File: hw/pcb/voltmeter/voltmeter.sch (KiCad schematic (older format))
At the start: 14 parts, among them J0 Screw_Terminal_01x02, K0 SPST Relay, K1 SPST Relay, K3 SPST Relay

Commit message: Updated circuit, added components, demo PCB layout. w/ Adam
Picked some parts and added them to the circuit. Implemented ADC circuit suggested by Nick.
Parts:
- removed D4: Red LED, symbol Device:LED
- removed K0, K1, K3: SPST Relay, symbol Relay:DIPxx-1Axx-11x
- removed R4: R, symbol Device:R
- removed U?: CA56-12EWA, Display_7Segment:CA56-12EWA, symbol Display_Character:CA56-12EWA
- added D3-x2, D3-x3: Green LED, symbol Device:LED
- added Q1, Q2: 2N7000, digikey-footprints:TO-92-3, symbol dk_Transistors-FETs-MOSFETs-Single:2N7000
- added R3-x2, R3-x3: R, symbol Device:R
- added U1: SN74HC595N, digikey-footprints:DIP-16_W7.62mm, symbol dk_Logic-Shift-Registers:SN74HC595N
- R1: value 20k -> 5k
- R2: value 49.9k -> 2k
- renumbered D3-x to D3-x1, R3-x to R3-x1
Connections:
- net labels added: 15vLeg, 30vLeg, 5vLeg, ADC
- wire segments 22 -> 31
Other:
- moved on the sheet: R3-x1

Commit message: Move to SMD parts; move to parts from Digikey library.
Move to SMD parts; move to parts from Digikey library. Schematic updates.
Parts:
- removed D0: 5.1V Zener, symbol Device:D_Zener
- removed D3-x1, D3-x2, D3-x3: Green LED, symbol Device:LED
- removed J0: Screw_Terminal_01x02, symbol Connector:Screw_Terminal_01x02
- removed Q1, Q2: 2N7000, digikey-footprints:TO-92-3, symbol dk_Transistors-FETs-MOSFETs-Single:2N7000
- removed U1: SN74HC595N, digikey-footprints:DIP-16_W7.62mm, symbol dk_Logic-Shift-Registers:SN74HC595N
- added D3-1, D3-2, D3-3: LTST-C150TBKT, digikey-footprints:1206, symbol dk_LED-Indication-Discrete:LTST-C150TBKT
- added J0: 1935161, digikey-footprints:Terminal_Block_D1.3mm_P5mm, symbol dk_Terminal-Blocks-Wire-to-Board:1935161
- added Q1, Q2: 2N7002, digikey-footprints:SOT-23-3, symbol dk_Transistors-FETs-MOSFETs-Single:2N7002
- R0, R1, R2: footprint (none) -> Resistor_SMD:R_0805_2012Metric_Pad1.15x1.40mm_HandSolder
- R3-1: renamed from R3-x1; value R -> 86.6; footprint (none) -> Resistor_SMD:R_0805_2012Metric_Pad1.15x1.40mm_HandSolder
- R3-2: renamed from R3-x2; value R -> 86.6; footprint (none) -> Resistor_SMD:R_0805_2012Metric_Pad1.15x1.40mm_HandSolder
- R3-3: renamed from R3-x3; value R -> 86.6; footprint (none) -> Resistor_SMD:R_0805_2012Metric_Pad1.15x1.40mm_HandSolder
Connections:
- net labels added: VoltageDivider

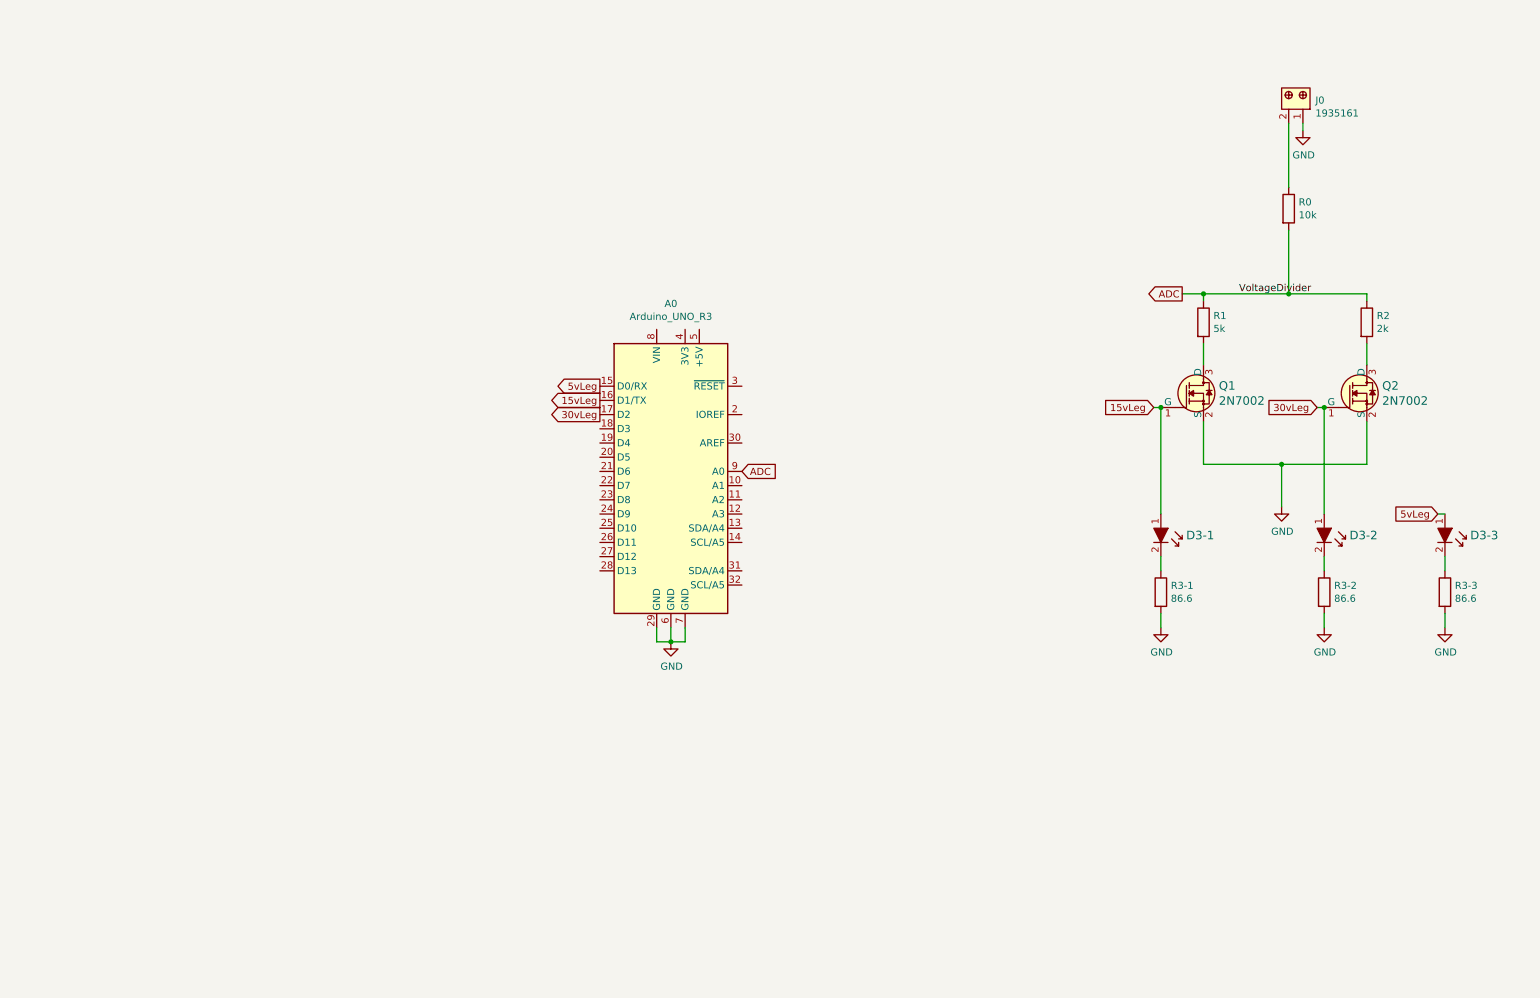
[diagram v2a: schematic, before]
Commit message: Changed to 4 voltage scales.
Changed design from 3-scale to 4-scale. Selected a few more parts and added them to the schematic.
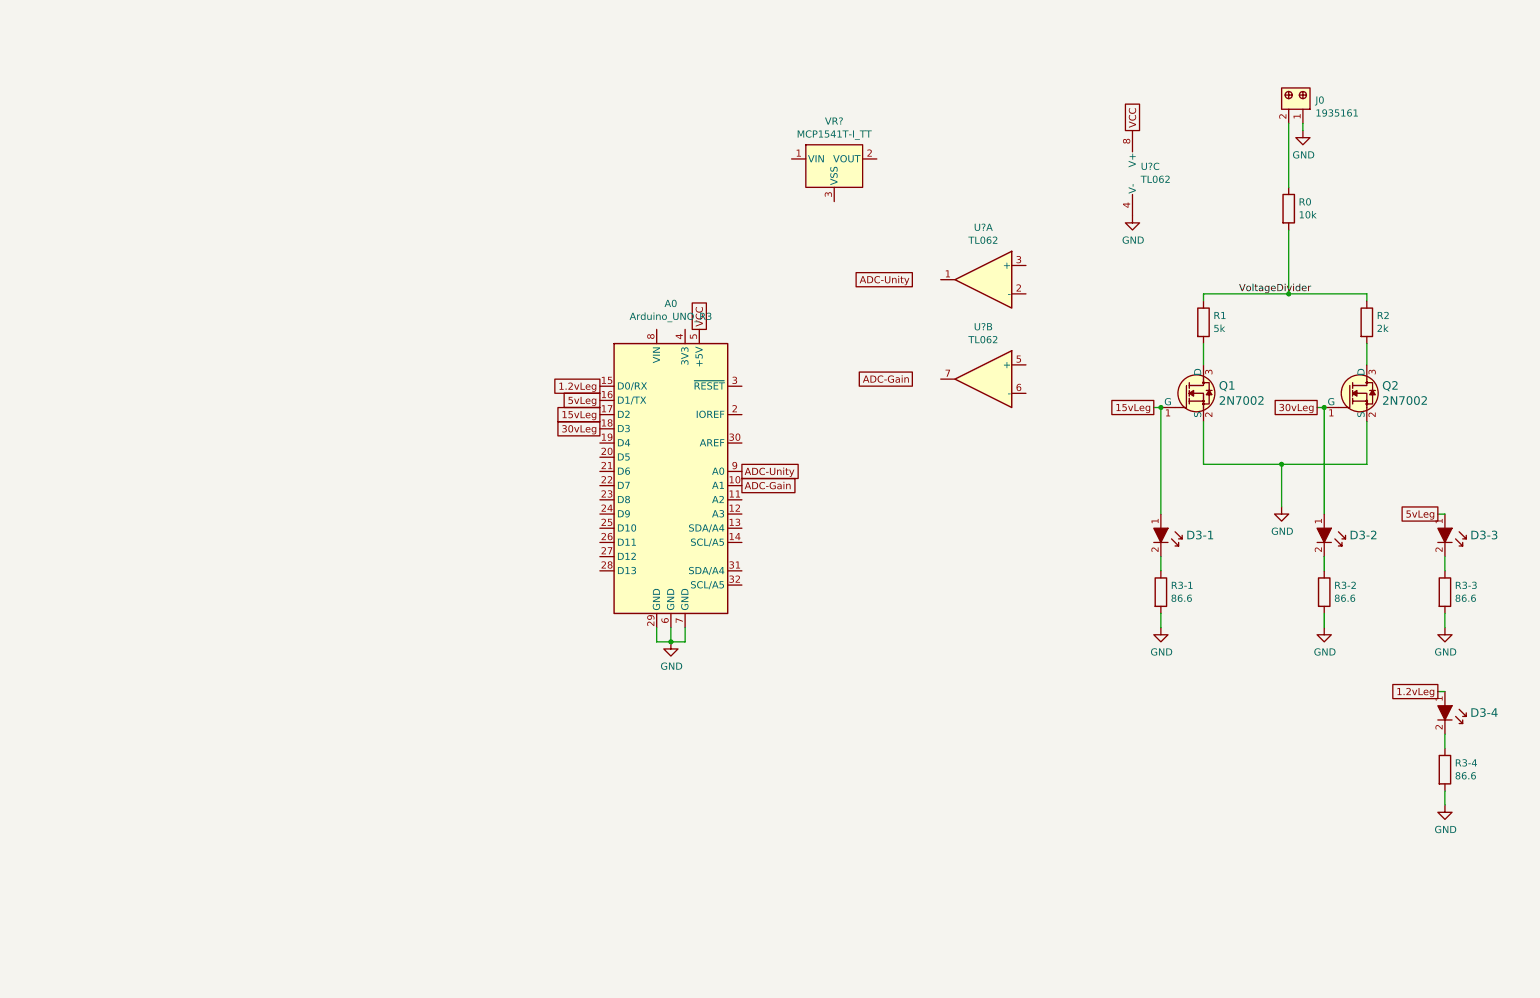
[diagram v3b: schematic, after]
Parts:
- added D3-4: LTST-C150TBKT, digikey-footprints:1206, symbol dk_LED-Indication-Discrete:LTST-C150TBKT
- added R3-4: 86.6, Resistor_SMD:R_0805_2012Metric_Pad1.15x1.40mm_HandSolder, symbol Device:R
- added U? (x3): TL062, footprints:TL062CDR, symbol Amplifier_Operational:TL062
- added VR?: MCP1541T-I_TT, digikey-footprints:SOT-23-3, symbol dk_PMIC-Voltage-Reference:MCP1541T-I_TT
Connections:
- net 15vLeg: now also A0.17 (D2); no longer A0.16 (D1/TX)
- net 30vLeg: now also A0.18 (D3); no longer A0.17 (D2)
- net 5vLeg: now also A0.16 (D1/TX); no longer A0.15 (D0/RX)
- net GND: now also R3-4.2, U?.4 (V-)
- net ADC-Gain: now reaches A0.10 (A1)
- net VCC: now reaches A0.5 (+5V)
- net VCC: now also U?.8 (V+)
- net ADC renamed VoltageDivider
- net VoltageDivider: no longer A0.9 (A0)
- new net: D3-4.2, R3-4.1
- new net 1.2vLeg: A0.15 (D0/RX), D3-4.1
- new net ADC-Unity: A0.9 (A0)
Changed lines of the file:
@@
 Wire Wire Line
 	8650 2850 8650 3600
-Text GLabel 8600 2850 0    50   Input ~ 0
+Text GLabel 8600 2850 0    50   UnSpc ~ 0
 15vLeg
-Text GLabel 9750 2850 0    50   Input ~ 0
+Text GLabel 9750 2850 0    50   UnSpc ~ 0
 30vLeg
-Text GLabel 4700 2800 0    50   Output ~ 0
+Text GLabel 4700 2900 0    50   UnSpc ~ 0
 15vLeg
-Text GLabel 4700 2900 0    50   Output ~ 0
+Text GLabel 4700 3000 0    50   UnSpc ~ 0
 30vLeg
 $Comp
@@
 Wire Wire Line
 	10650 3900 10650 4000
-Text GLabel 10600 3600 0    50   Input ~ 0
+Text GLabel 10600 3600 0    50   UnSpc ~ 0
 5vLeg
-Text GLabel 4700 2700 0    50   Output ~ 0
+Text GLabel 4700 2800 0    50   UnSpc ~ 0
 5vLeg
 Wire Wire Line
 	9550 1300 9550 850
-Text GLabel 8800 2050 0    50   Output ~ 0
-ADC
-Text GLabel 5700 3300 2    50   Input ~ 0
-ADC
-Wire Wire Line
-	8800 2050 8950 2050
-Connection ~ 8950 2050
+Text GLabel 6900 1950 0    50   UnSpc ~ 0
+ADC-Unity
+Text GLabel 5700 3300 2    50   UnSpc ~ 0
+ADC-Unity
 Wire Wire Line
 	8600 2850 8650 2850
@@
 Text Label 9200 2050 0    50   ~ 0
 VoltageDivider
+$Comp
+L dk_PMIC-Voltage-Reference:MCP1541T-I_TT VR?
+U 1 1 5F4868C2
+P 6350 1100
+F 0 "VR?" H 6350 1365 50  0000 C CNN
+F 1 "MCP1541T-I_TT" H 6350 1274 50  0000 C CNN
+F 2 "digikey-footprints:SOT-23-3" H 6550 1300 60  0001 L CNN
+F 3 "http://www.microchip.com/mymicrochip/filehandler.aspx?ddocname=en011331" H 6550 1400 60  0001 L CNN
+F 4 "MCP1541T-I/TTCT-ND" H 6550 1500 60  0001 L CNN "Digi-Key_PN"
+F 5 "MCP1541T-I/TT" H 6550 1600 60  0001 L CNN "MPN"
+F 6 "Integrated Circuits (ICs)" H 6550 1700 60  0001 L CNN "Category"
+F 7 "PMIC - Voltage Reference" H 6550 1800 60  0001 L CNN "Family"
+F 8 "http://www.microchip.com/mymicrochip/filehandler.aspx?ddocname=en011331" H 6550 1900 60  0001 L CNN "DK_Datasheet_Link"
+F 9 "/product-detail/en/microchip-technology/MCP1541T-I-TT/MCP1541T-I-TTCT-ND/1979818" H 6550 2000 60  0001 L CNN "DK_Detail_Page"
+F 10 "IC VREF SERIES 4.096V SOT23-3" H 6550 2100 60  0001 L CNN "Description"
+F 11 "Microchip Technology" H 6550 2200 60  0001 L CNN "Manufacturer"
+F 12 "Active" H 6550 2300 60  0001 L CNN "Status"
+	1    6350 1100
+	1    0    0    -1
+$EndComp
+$Comp
+L power:GND #PWR0107
+U 1 1 5F4BD11F
+P 8450 1500
+F 0 "#PWR0107" H 8450 1250 50  0001 C CNN
+F 1 "GND" H 8455 1327 50  0000 C CNN
+F 2 "" H 8450 1500 50  0001 C CNN
+F 3 "" H 8450 1500 50  0001 C CNN
+	1    8450 1500
+	1    0    0    -1
+$EndComp
+Text GLabel 5400 2300 1    50   UnSpc ~ 0
+VCC
+Text GLabel 8450 900  1    50   UnSpc ~ 0
+VCC
+$Comp
+L Device:R R3-4
+U 1 1 5F4CB52D
+P 10650 5400
+F 0 "R3-4" H 10720 5446 50  0000 L CNN
+F 1 "86.6" H 10720 5355 50  0000 L CNN
+F 2 "Resistor_SMD:R_0805_2012Metric_Pad1.15x1.40mm_HandSolder" V 10580 5400 50  0001 C CNN
+F 3 "~" H 10650 5400 50  0001 C CNN
+	1    10650 5400
+	1    0    0    -1
+$EndComp
+$Comp
+L power:GND #PWR0108
+U 1 1 5F4CB533
+P 10650 5650
+F 0 "#PWR0108" H 10650 5400 50  0001 C CNN
+F 1 "GND" H 10655 5477 50  0000 C CNN
+F 2 "" H 10650 5650 50  0001 C CNN
+F 3 "" H 10650 5650 50  0001 C CNN
+	1    10650 5650
+	1    0    0    -1
+$EndComp
+Wire Wire Line
+	10650 5550 10650 5650
+Wire Wire Line
+	10650 5150 10650 5250
+Text GLabel 10600 4850 0    50   UnSpc ~ 0
+1.2vLeg
+Wire Wire Line
+	10600 4850 10650 4850
+$Comp
+L dk_LED-Indication-Discrete:LTST-C150TBKT D3-4
+U 1 1 5F4CB546
+P 10650 5050
+F 0 "D3-4" V 10600 5228 60  0000 L CNN
+F 1 "LTST-C150TBKT" V 10653 5228 60  0001 L CNN
+F 2 "digikey-footprints:1206" H 10850 5250 60  0001 L CNN
+F 3 "http://optoelectronics.liteon.com/upload/download/DS22-2000-026/LTST-C150TBKT(0630).pdf" H 10850 5350 60  0001 L CNN
+F 4 "160-1643-1-ND" H 10850 5450 60  0001 L CNN "Digi-Key_PN"
+F 5 "LTST-C150TBKT" H 10850 5550 60  0001 L CNN "MPN"
+F 6 "Optoelectronics" H 10850 5650 60  0001 L CNN "Category"
+F 7 "LED Indication - Discrete" H 10850 5750 60  0001 L CNN "Family"
+F 8 "http://optoelectronics.liteon.com/upload/download/DS22-2000-026/LTST-C150TBKT(0630).pdf" H 10850 5850 60  0001 L CNN "DK_Datasheet_Link"
+F 9 "/product-detail/en/lite-on-inc/LTST-C150TBKT/160-1643-1-ND/573584" H 10850 5950 60  0001 L CNN "DK_Detail_Page"
+F 10 "LED BLUE CLEAR 1206 SMD" H 10850 6050 60  0001 L CNN "Description"
+F 11 "Lite-On Inc." H 10850 6150 60  0001 L CNN "Manufacturer"
+F 12 "Active" H 10850 6250 60  0001 L CNN "Status"
+	1    10650 5050
+	0    1    1    0
+$EndComp
+Text GLabel 4700 2700 0    50   UnSpc ~ 0
+1.2vLeg
+Text GLabel 5700 3400 2    50   UnSpc ~ 0
+ADC-Gain
+Text GLabel 6900 2650 0    50   UnSpc ~ 0
+ADC-Gain
+$Comp
+L Amplifier_Operational:TL062 U?
+U 1 1 5F4CF15C
+P 7400 1950
+F 0 "U?" H 7400 2317 50  0000 C CNN
+F 1 "TL062" H 7400 2226 50  0000 C CNN
+F 2 "footprints:TL062CDR" H 7400 1950 50  0001 C CNN
+F 3 "http://www.ti.com/lit/ds/symlink/tl061.pdf" H 7400 1950 50  0001 C CNN
+	1    7400 1950
+	-1   0    0    -1
+$EndComp
+$Comp
+L Amplifier_Operational:TL062 U?
+U 2 1 5F4D172B
+P 7400 2650
+F 0 "U?" H 7400 3017 50  0000 C CNN
+F 1 "TL062" H 7400 2926 50  0000 C CNN
+F 2 "footprints:TL062CDR" H 7400 2650 50  0001 C CNN
+F 3 "http://www.ti.com/lit/ds/symlink/tl061.pdf" H 7400 2650 50  0001 C CNN
+	2    7400 2650
+	-1   0    0    -1
+$EndComp
+$Comp
+L Amplifier_Operational:TL062 U?
+U 3 1 5F4D3B6F
+P 8550 1200
+F 0 "U?" H 8508 1246 50  0000 L CNN
+F 1 "TL062" H 8508 1155 50  0000 L CNN
+F 2 "footprints:TL062CDR" H 8550 1200 50  0001 C CNN
+F 3 "http://www.ti.com/lit/ds/symlink/tl061.pdf" H 8550 1200 50  0001 C CNN
+	3    8550 1200
+	1    0    0    -1
+$EndComp
 $EndSCHEMATC

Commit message: Finished the schematic!
Added 7-segment display, op-amps, and completed resistors and capacitors for ICs. First pass at the schematic is complete!
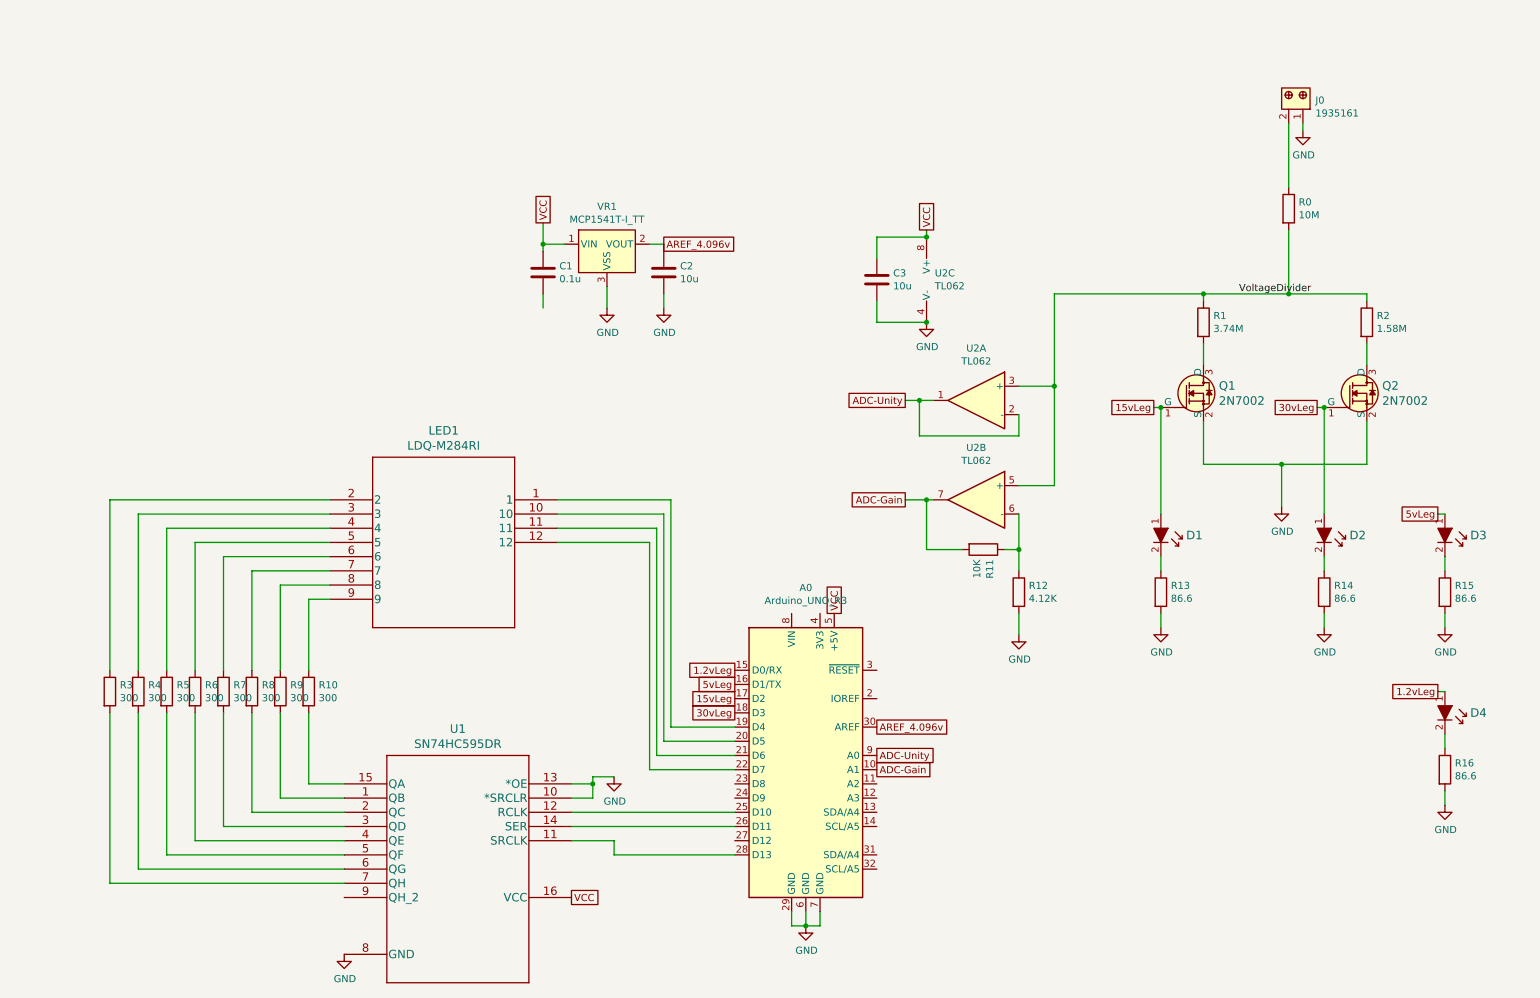
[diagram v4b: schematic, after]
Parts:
- added C1: 0.1u, Capacitor_SMD:C_0805_2012Metric_Pad1.15x1.40mm_HandSolder, symbol Device:C
- added C2, C3: 10u, Capacitor_SMD:C_0805_2012Metric_Pad1.15x1.40mm_HandSolder, symbol Device:C
- added LED1: LDQ-M284RI, footprints3:LDQ-M284RI, symbol 2020-08-31_02-39-33:LDQ-M284RI
- added R10, R3, R4, R5, R6, R7, R8, R9: 300, Resistor_SMD:R_0805_2012Metric_Pad1.15x1.40mm_HandSolder, symbol Device:R
- added R11: 10K, Resistor_SMD:R_0805_2012Metric_Pad1.15x1.40mm_HandSolder, symbol Device:R
- added R12: 4.12K, Resistor_SMD:R_0805_2012Metric_Pad1.15x1.40mm_HandSolder, symbol Device:R
- added U1: SN74HC595DR, footprints2:SN74HC595DR, symbol 2020-08-31_02-24-53:SN74HC595DR
- R0: value 10k -> 10M
- R1: value 5k -> 3.74M
- R2: value 2k -> 1.58M
- gave numbers to parts that had none: 2
- renumbered D3-1 to D1, D3-2 to D2, D3-3 to D3, D3-4 to D4, R3-1 to R13, R3-2 to R14, R3-3 to R15, R3-4 to R16
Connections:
- net ADC-Gain: now also U2.7, R11.2
- net ADC-Unity: now also U2.1, U2.2 (-)
- net GND: now also VR1.3 (VSS), C2.2, C3.2, R12.2, U1.10 (*SRCLR), U1.13 (*OE), U1.8 (GND)
- net VCC: now also VR1.1 (VIN), C1.1, C3.1, U1.16 (VCC)
- net VoltageDivider: now also U2.3 (+), U2.5 (+)
- net at A0.19 (D4): now also LED1.1
- net at A0.20 (D5): now also LED1.10
- net at A0.21 (D6): now also LED1.11
- net at A0.22 (D7): now also LED1.12
- net at A0.25 (D10): now also U1.12 (RCLK)
- net at A0.26 (D11): now also U1.14 (SER)
- net at A0.28 (D13): now also U1.11 (SRCLK)
- net AREF_4.096v: now reaches A0.30 (AREF)
- net AREF_4.096v: now also VR1.2 (VOUT), C2.1
- net at U2.6 (-): now also R11.1, R12.1
- new net: R9.2, U1.1 (QB)
- new net: R10.2, U1.15 (QA)
- new net: R8.2, U1.2 (QC)
- new net: R7.2, U1.3 (QD)
- new net: R6.2, U1.4 (QE)
- new net: R5.2, U1.5 (QF)
- new net: R4.2, U1.6 (QG)
- new net: R3.2, U1.7 (QH)
- new net: LED1.2, R3.1
- new net: LED1.3, R4.1
- new net: LED1.4, R5.1
- new net: LED1.5, R6.1
- new net: LED1.6, R7.1
- new net: LED1.7, R8.1
- new net: LED1.8, R9.1
- new net: LED1.9, R10.1
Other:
- moved on the sheet: A0, U2A, U2B, U2C, VR1

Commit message: Fix as many DRC errors as possible.
Fixed DRC errors by marking unused pins and editing pin directionality on some schematic symbols.
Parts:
- removed A0: Arduino_UNO_R3, Module:Arduino_UNO_R3, symbol MCU_Module:Arduino_UNO_R3
- added A0: Arduino_UNO_R3_SHIELD, Module:Arduino_UNO_R3, symbol marks_library:Arduino_UNO_R3_SHIELD
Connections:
- net 1.2vLeg: now also A0.15 (D0/RX)
- net 15vLeg: now also A0.17 (D2)
- net 30vLeg: now also A0.18 (D3)
- net 5vLeg: now also A0.16 (D1/TX)
- net ADC-Gain: now also A0.10 (A1)
- net ADC-Unity: now also A0.9 (A0)
- net AREF_4.096v: now also A0.30 (AREF)
- net GND: now also C1.2, A0.29 (GND), A0.6 (GND), A0.7 (GND)
- net VCC: now also A0.5 (+5V)
- net at LED1.1: now also A0.19 (D4)
- net at LED1.10: now also A0.20 (D5)
- net at LED1.11: now also A0.21 (D6)
- net at LED1.12: now also A0.22 (D7)
- net at U1.12 (RCLK): now also A0.25 (D10)
- net at U1.14 (SER): now also A0.26 (D11)
- net at U1.11 (SRCLK): now also A0.28 (D13)
- no-connect marks 0 -> 14
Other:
- moved on the sheet: R10, R3, R4, R5, R6, R7, R8, R9

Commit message: Begin PCB layout.
Begin PCB layout. Edit Arduino footprint to better reflect the fact that it's just the header pins.
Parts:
- A0: footprint Module:Arduino_UNO_R3 -> marks_footprint_library:Arduino_UNO_R3_SHIELD
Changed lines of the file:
@@
 F 0 "A0" H 6150 6481 50  0000 C CNN
 F 1 "Arduino_UNO_R3_SHIELD" H 6150 6390 50  0000 C CNN
-F 2 "Module:Arduino_UNO_R3" H 6150 5300 50  0001 C CIN
+F 2 "marks_footprint_library:Arduino_UNO_R3_SHIELD" H 6150 5300 50  0001 C CIN
 F 3 "https://www.arduino.cc/en/Main/arduinoBoardUno" H 6150 5300 50  0001 C CNN
 	1    6150 5300
